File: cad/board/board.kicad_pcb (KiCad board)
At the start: 4 copper layers, 65 x 30 mm, 47 parts, among them IC1 MAX17048G+T10, J1 USB_C_Receptacle_USB2.0_16P, J2 LiPo (min 500mAh), J3 Conn_02x11_Odd_Even, Q1 DMP2045U, U1 ESP32-C6-MINI-1, U2 USBLC6-2SC6, U3 AP2112K-3.3, U4 MCP73831-2-OT

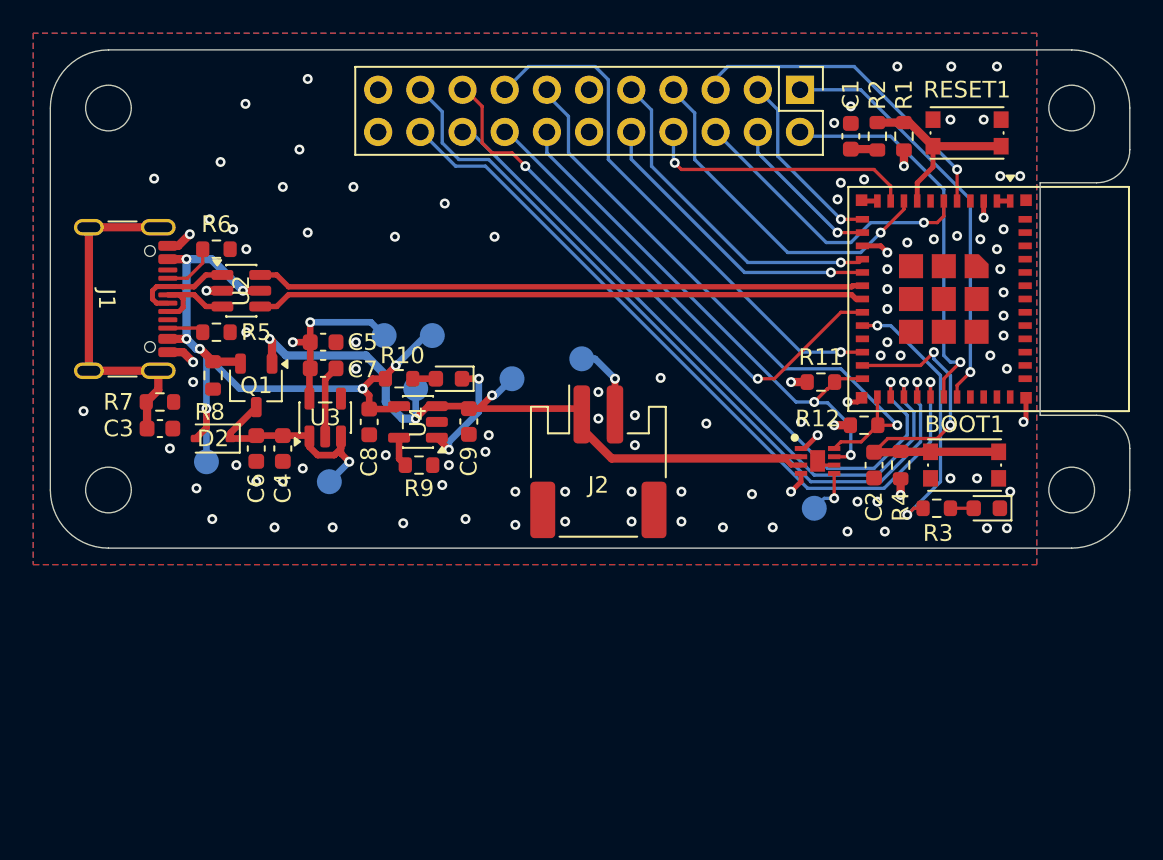
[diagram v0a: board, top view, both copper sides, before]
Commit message: Extend board to include new peripherals
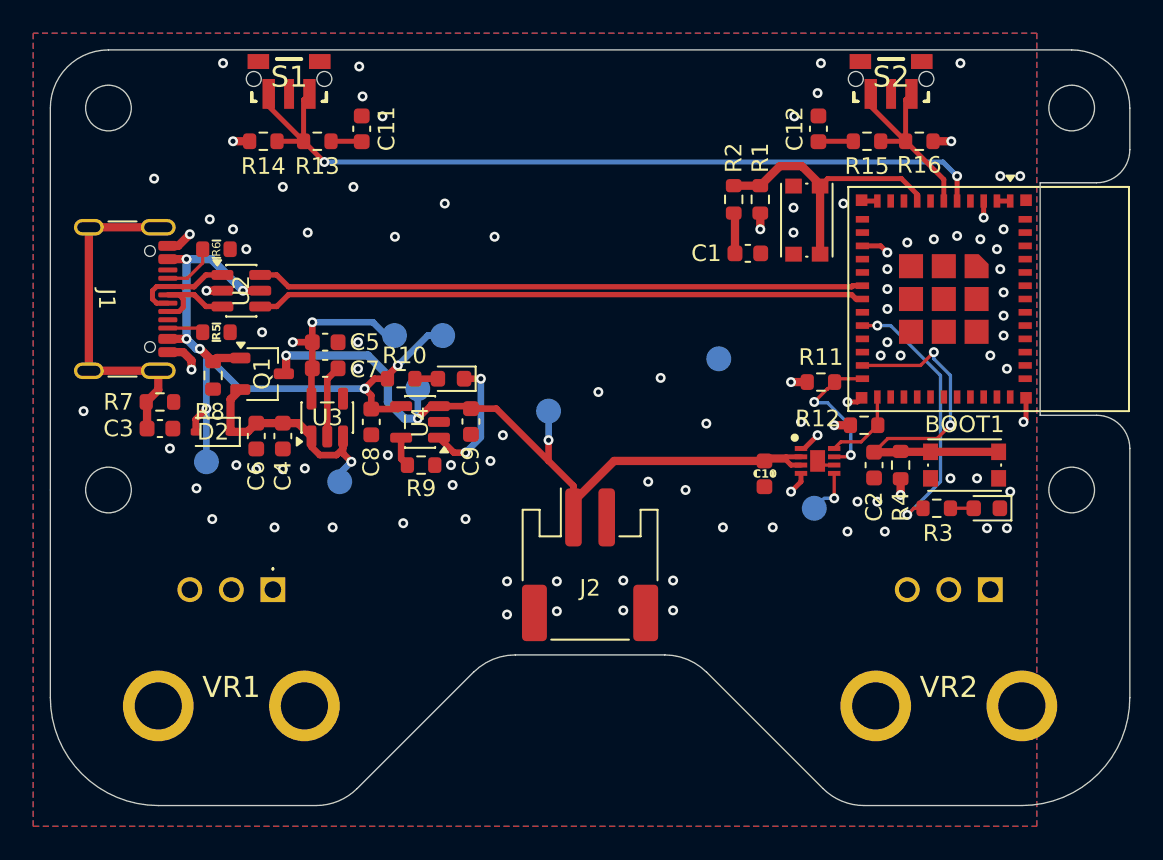
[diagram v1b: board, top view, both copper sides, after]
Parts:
- removed J3: Conn_02x11_Odd_Even, Connector_PinHeader_2.54mm:PinHeader_2x11_P2.54mm_Vertical
- added C10: 100nF, Capacitor_SMD:C_0603_1608Metric, F.Cu at (118.0, 105.5)
- added C11: 1uF, Capacitor_SMD:C_0603_1608Metric, F.Cu at (93.8, 84.8)
- added C12: 1uF, Capacitor_SMD:C_0603_1608Metric, F.Cu at (121.2, 84.8)
- added R13: 100, Resistor_SMD:R_0603_1608Metric, F.Cu at (91.1, 85.5)
- added R14: 10K, Resistor_SMD:R_0603_1608Metric, F.Cu at (87.8, 85.5)
- added R15: 100, Resistor_SMD:R_0603_1608Metric, F.Cu at (124.2, 85.5)
- added R16: 10K, Resistor_SMD:R_0603_1608Metric, F.Cu at (127.3, 85.5)
- added S1: PTS845VM20PSMTR4_LFS, Imports:PTS845VM20PSMTR4LFS, F.Cu at (89.4, 81.8)
- added S2: PTS845VM20PSMTR4_LFS, Imports:PTS845VM20PSMTR4LFS, F.Cu at (125.6, 81.8)
- added VR1: PTV09A-4220U-B103, Imports:PTV09A4220FB103, F.Cu at (88.4, 112.5)
- added VR2: PTV09A-4220U-B103, Imports:PTV09A4220FB103, F.Cu at (131.6, 112.5)
- R10: value 1k -> 1K
- R11, R12: value 10k -> 4.7K
- R5, R6: value 5.1k -> 5.1K
- R8: value 10k -> 10K
- R9: value 2k -> 2K
- moved RESET1 11.0 mm to (120.5, 90.2), turned to -90 degrees
- moved R1 9.45 mm to (117.8, 89.0)
- moved R2 9.45 mm to (116.2, 89.0)
- moved C1 9.39 mm to (117.0, 92.2), turned to 0 degrees
- moved TP8 8.25 mm to (115.2, 98.6)
- moved J2 6.22 mm to (107.5, 111.0)
- moved TP6 2.94 mm to (105.0, 101.8)
- moved Q1 0.78 mm to (87.8, 99.5), turned to 0 degrees
- moved C4 0.75 mm to (89.0, 103.2)
- moved C6 0.75 mm to (87.4, 103.2)
- moved TP4 0.62 mm to (92.4, 106.0)
- moved TP5 0.62 mm to (95.7, 97.2)
- moved TP7 0.62 mm to (98.6, 97.2)
- moved D2 0.40 mm to (84.8, 103.0)
- moved C5 0.12 mm to (91.5, 97.6)
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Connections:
- Q1 pad 1: VBAT -> VBUS
- Q1 pad 2: VBUS -> Net-(D2-K)
- Q1 pad 3: Net-(D2-K) -> VBAT
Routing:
- net IO22: track 47.1 -> 0.00 mm, vias 1 -> 0
- net IO23: track 45.3 -> 0.00 mm, vias 1 -> 0
- net IO20: track 42.9 -> 0.00 mm, vias 2 -> 0
- net IO21: track 41.2 -> 0.00 mm, vias 1 -> 0
- net SDA: track 37.0 -> 4.92 mm, vias 1 -> 0
- net IO8: track 32.1 -> 0.00 mm, vias 1 -> 0
- net IO2: track 20.0 -> 50.0 mm, vias 1 -> 2
- net IO14: track 29.4 -> 0.00 mm, vias 1 -> 0
- net TX: track 25.2 -> 0.00 mm, vias 1 -> 0
- net RX: track 23.8 -> 0.00 mm, vias 1 -> 0
- net SCL: track 32.6 -> 9.07 mm
- net IO4: track 21.2 -> 0.00 mm, vias 1 -> 0
- net IO6: track 20.3 -> 0.00 mm, vias 1 -> 0
- net IO7: track 18.4 -> 0.00 mm, vias 1 -> 0
- net IO5: track 16.4 -> 0.00 mm, vias 1 -> 0
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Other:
- board size 65 x 30 mm -> 65 x 45.5 mm
